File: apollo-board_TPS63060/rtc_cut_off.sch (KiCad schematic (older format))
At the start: 17 parts, among them J6 Conn_01x02_Male, Q6 BSS84-7-F, SW1 DNP/SKRKAEE020, U5 RV-3028-C7, U8 TPS70933DRVT

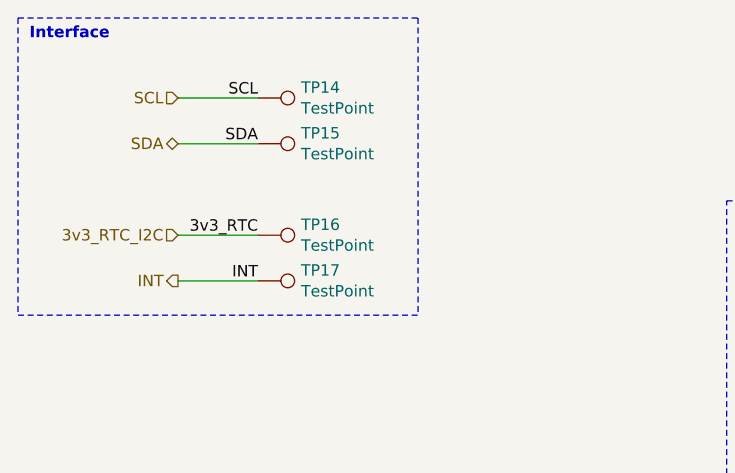
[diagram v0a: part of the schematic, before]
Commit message: Remove unused parts at schematic level.
+ solve schematic DRC issues
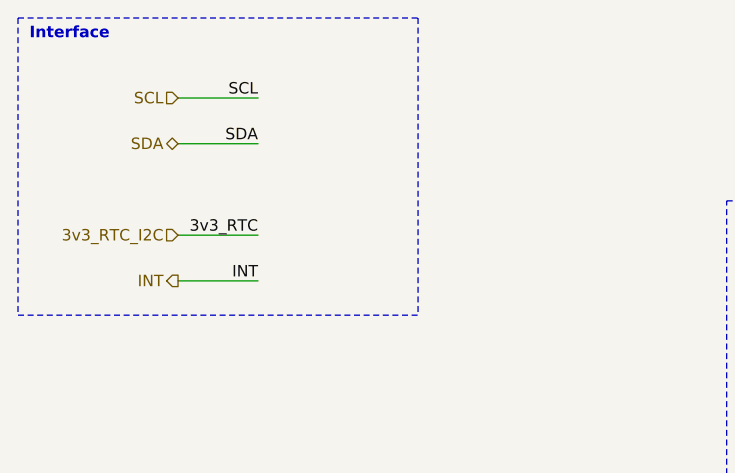
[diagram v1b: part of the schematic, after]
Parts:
- removed TP14, TP15, TP16, TP17: TestPoint, TestPoint:TestPoint_Pad_D1.0mm, symbol Connector:TestPoint
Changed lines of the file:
@@
 Text Notes 6400 1750 2    50   Italic 0
 External trigger\nswitch on board (optional)
-$Comp
-L Connector:TestPoint TP14
-U 1 1 5FD6FC2A
-P 1600 900
-F 0 "TP14" V 1554 1088 50  0000 L CNN
-F 1 "TestPoint" V 1645 1088 50  0000 L CNN
-F 2 "TestPoint:TestPoint_Pad_D1.0mm" H 1800 900 50  0001 C CNN
-F 3 "~" H 1800 900 50  0001 C CNN
-	1    1600 900
-	0    1    1    0
-$EndComp
-$Comp
-L Connector:TestPoint TP15
-U 1 1 5FD6FEB6
-P 1600 1100
-F 0 "TP15" V 1554 1288 50  0000 L CNN
-F 1 "TestPoint" V 1645 1288 50  0000 L CNN
-F 2 "TestPoint:TestPoint_Pad_D1.0mm" H 1800 1100 50  0001 C CNN
-F 3 "~" H 1800 1100 50  0001 C CNN
-	1    1600 1100
-	0    1    1    0
-$EndComp
-$Comp
-L Connector:TestPoint TP16
-U 1 1 5FD700CA
-P 1600 1500
-F 0 "TP16" V 1554 1688 50  0000 L CNN
-F 1 "TestPoint" V 1645 1688 50  0000 L CNN
-F 2 "TestPoint:TestPoint_Pad_D1.0mm" H 1800 1500 50  0001 C CNN
-F 3 "~" H 1800 1500 50  0001 C CNN
-	1    1600 1500
-	0    1    1    0
-$EndComp
-$Comp
-L Connector:TestPoint TP17
-U 1 1 5FD702E9
-P 1600 1700
-F 0 "TP17" V 1554 1888 50  0000 L CNN
-F 1 "TestPoint" V 1645 1888 50  0000 L CNN
-F 2 "TestPoint:TestPoint_Pad_D1.0mm" H 1800 1700 50  0001 C CNN
-F 3 "~" H 1800 1700 50  0001 C CNN
-	1    1600 1700
-	0    1    1    0
-$EndComp
 Wire Notes Line
 	550  550  2300 550

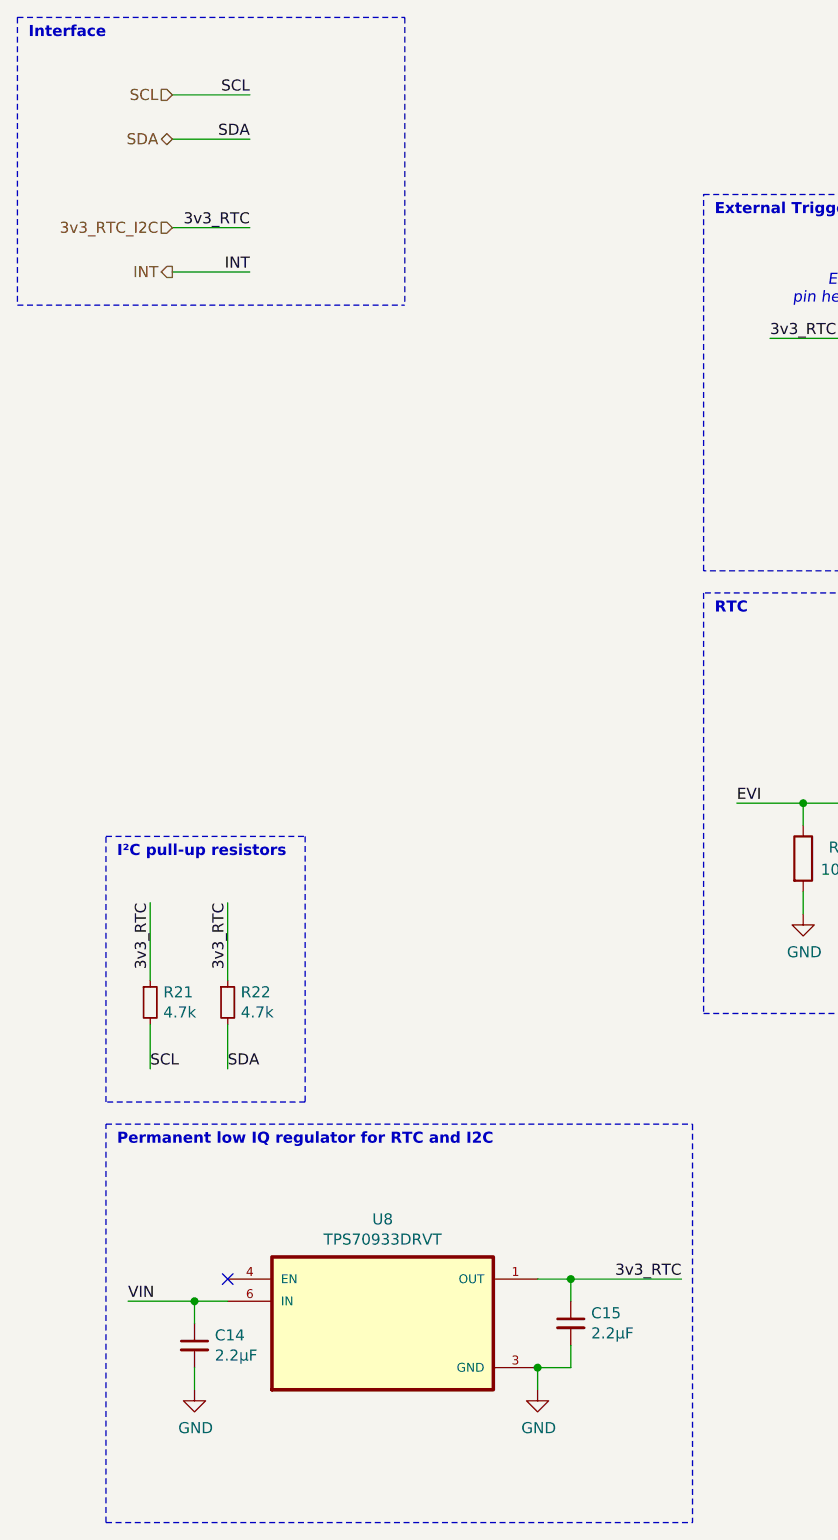
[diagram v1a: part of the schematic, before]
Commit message: Recreate TPS709 symbol to and set footprint to SOT23-5
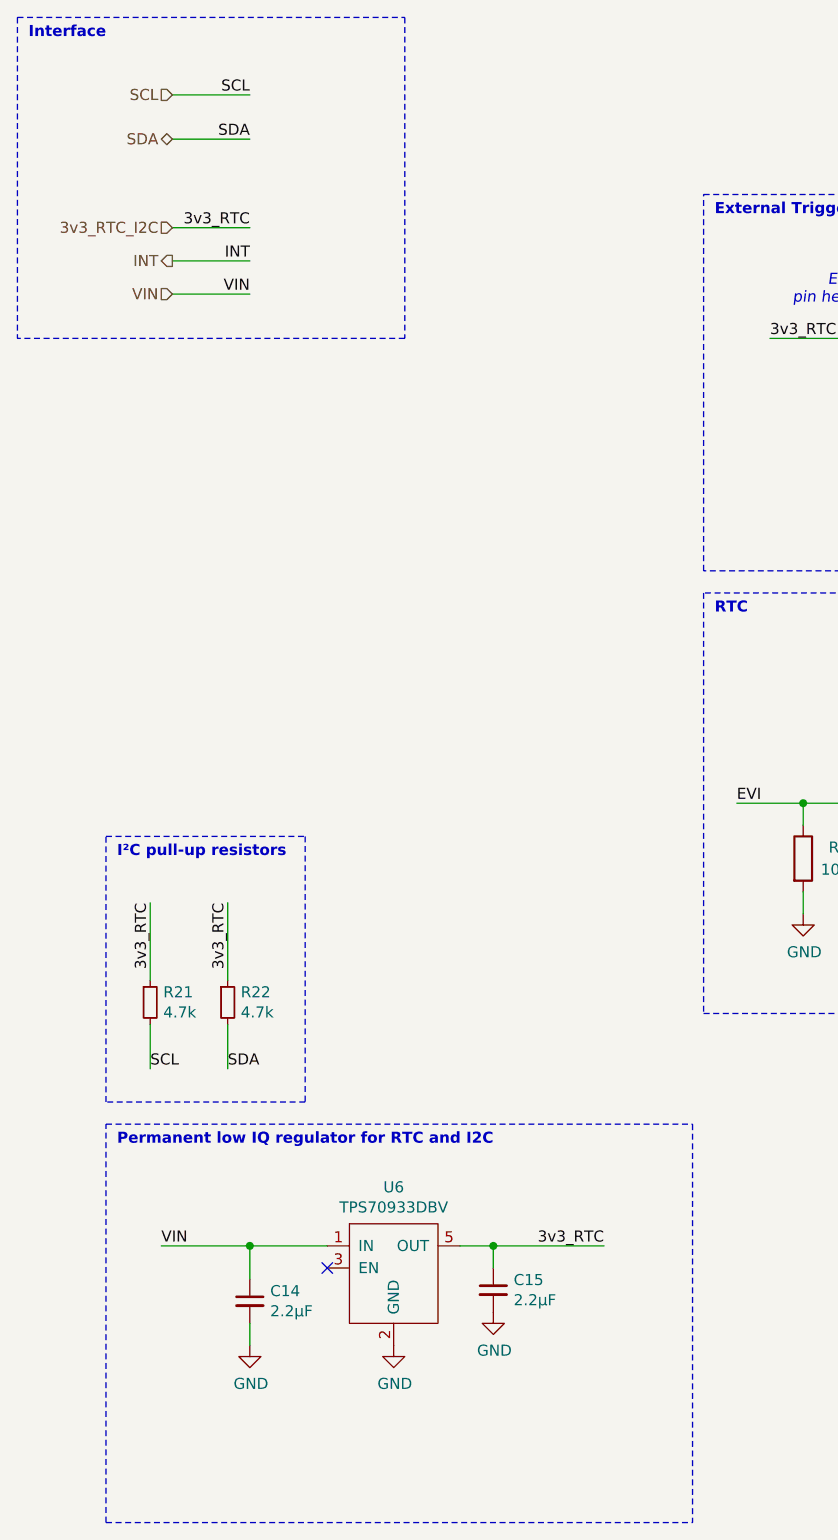
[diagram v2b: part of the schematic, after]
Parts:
- removed U8: TPS70933DRVT, Package_TO_SOT_SMD:SOT-23-6, symbol TPS70933DRV:TPS70933DRVT
- added U6: TPS70933DBV, Package_TO_SOT_SMD:SOT-23-5, symbol TPS70933DRV:TPS70933DBV
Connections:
- net 3v3_RTC_I2C: now also U6.5 (OUT)
- net GND: now also U6.2 (GND)
- net VIN: now also U6.1 (IN)
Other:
- moved on the sheet: C14, C15
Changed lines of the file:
@@
 Text HLabel 1250 1100 0    50   BiDi ~ 0
 SDA
-Text HLabel 1250 1700 0    50   Output ~ 0
+Text HLabel 1250 1650 0    50   Output ~ 0
 INT
 NoConn ~ 6150 4300
@@
 Text Label 1600 1100 2    50   ~ 0
 SDA
-Text Label 1600 1700 2    50   ~ 0
+Text Label 1600 1650 2    50   ~ 0
 INT
 Wire Wire Line
-	1250 1700 1600 1700
+	1250 1650 1600 1650
 Wire Wire Line
 	1250 900  1600 900
@@
 Wire Notes Line
 	550  550  2300 550
-Wire Notes Line
-	2300 550  2300 1850
-Wire Notes Line
-	550  1850 2300 1850
-Wire Notes Line
-	550  550  550  1850
 Text Label 7350 3550 2    50   ~ 0
 3v3_RTC
@@
 	6900 3550 6250 3550
 Connection ~ 6900 3550
-Wire Wire Line
-	1350 6350 1500 6350
-Wire Wire Line
-	1050 6350 1350 6350
-Text Label 1050 6350 0    50   ~ 0
-VIN
-Connection ~ 1350 6350
-Wire Wire Line
-	1350 6350 1350 6450
-$Comp
-L power:GND #PWR?
-U 1 1 5FE9A849
-P 1350 6750
-AR Path="/5F63A0E9/5FE9A849" Ref="#PWR?"  Part="1"
-AR Path="/5F63A00B/5FE9A849" Ref="#PWR0102"  Part="1"
-F 0 "#PWR0102" H 1350 6500 50  0001 C CNN
-F 1 "GND" H 1355 6577 50  0000 C CNN
-F 2 "" H 1350 6750 50  0001 C CNN
-F 3 "" H 1350 6750 50  0001 C CNN
-	1    1350 6750
-	1    0    0    -1
-$EndComp
-$Comp
-L power:GND #PWR?
-U 1 1 5FE9A84F
-P 2900 6750
-AR Path="/5F63A0E9/5FE9A84F" Ref="#PWR?"  Part="1"
-AR Path="/5F63A00B/5FE9A84F" Ref="#PWR0103"  Part="1"
-F 0 "#PWR0103" H 2900 6500 50  0001 C CNN
-F 1 "GND" H 2905 6577 50  0000 C CNN
-F 2 "" H 2900 6750 50  0001 C CNN
-F 3 "" H 2900 6750 50  0001 C CNN
-	1    2900 6750
-	1    0    0    -1
-$EndComp
-Text Label 3550 6250 2    50   ~ 0
-3v3_RTC
-Wire Wire Line
-	3050 6550 3050 6650
-Wire Wire Line
-	3050 6650 2900 6650
-Connection ~ 2900 6650
-Wire Wire Line
-	3050 6350 3050 6250
-Wire Wire Line
-	2900 6750 2900 6650
-Wire Wire Line
-	1350 6650 1350 6750
-NoConn ~ 1500 6250
-Wire Notes Line
-	950  7350 950  5550
-Wire Wire Line
-	2900 6250 3050 6250
-Connection ~ 3050 6250
-$Comp
-L Device:C_Small C?
-U 1 1 5FE9A860
-P 3050 6450
-AR Path="/5F63A0E9/5FE9A860" Ref="C?"  Part="1"
-AR Path="/5F63A00B/5FE9A860" Ref="C15"  Part="1"
-F 0 "C15" H 3142 6496 50  0000 L CNN
-F 1 "2.2μF" H 3142 6405 50  0000 L CNN
-F 2 "Capacitor_SMD:C_0603_1608Metric" H 3050 6450 50  0001 C CNN
-F 3 "~" H 3050 6450 50  0001 C CNN
-	1    3050 6450
-	1    0    0    -1
-$EndComp
-$Comp
-L Device:C_Small C?
-U 1 1 5FE9A866
-P 1350 6550
-AR Path="/5F63A0E9/5FE9A866" Ref="C?"  Part="1"
-AR Path="/5F63A00B/5FE9A866" Ref="C14"  Part="1"
-F 0 "C14" H 1442 6596 50  0000 L CNN
-F 1 "2.2μF" H 1442 6505 50  0000 L CNN
-F 2 "Capacitor_SMD:C_0603_1608Metric" H 1350 6550 50  0001 C CNN
-F 3 "~" H 1350 6550 50  0001 C CNN
-	1    1350 6550
-	1    0    0    -1
-$EndComp
-$Comp
-L TPS70933DRV:TPS70933DRVT U?
-U 1 1 5FE9A86C
-P 2200 6450
-AR Path="/5F63A0E9/5FE9A86C" Ref="U?"  Part="1"
-AR Path="/5F63A00B/5FE9A86C" Ref="U8"  Part="1"
-F 0 "U8" H 2200 6920 50  0000 C CNN
-F 1 "TPS70933DRVT" H 2200 6829 50  0000 C CNN
-F 2 "Package_TO_SOT_SMD:SOT-23-6" H 2200 6450 50  0001 L BNN
-F 3 "https://www.ti.com/lit/gpn/tps709" H 2200 6450 50  0001 L BNN
-	1    2200 6450
-	1    0    0    -1
-$EndComp
-Wire Wire Line
-	3050 6250 3550 6250
-Text Notes 1000 5650 0    50   ~ 10
-Permanent low IQ regulator for RTC and I2C
-Wire Notes Line
-	950  7350 3600 7350
-Wire Notes Line
-	950  5550 3600 5550
-Wire Notes Line
-	3600 5550 3600 7350
 Wire Notes Line
 	7500 5050 7500 3150
@@
 Text Notes 7650 3300 0    50   ~ 10
 Reverse ~INT~ of the RTC
+Wire Notes Line
+	3600 5550 3600 7350
+Wire Notes Line
+	950  5550 3600 5550
+Wire Notes Line
+	950  7350 3600 7350
+Text Notes 1000 5650 0    50   ~ 10
+Permanent low IQ regulator for RTC and I2C
+$Comp
+L Device:C_Small C?
+U 1 1 5FE9A866
+P 1600 6350
+AR Path="/5F63A0E9/5FE9A866" Ref="C?"  Part="1"
+AR Path="/5F63A00B/5FE9A866" Ref="C14"  Part="1"
+F 0 "C14" H 1692 6396 50  0000 L CNN
+F 1 "2.2μF" H 1692 6305 50  0000 L CNN
+F 2 "Capacitor_SMD:C_0603_1608Metric" H 1600 6350 50  0001 C CNN
+F 3 "~" H 1600 6350 50  0001 C CNN
+	1    1600 6350
+	1    0    0    -1
+$EndComp
+$Comp
+L Device:C_Small C?
+U 1 1 5FE9A860
+P 2700 6300
+AR Path="/5F63A0E9/5FE9A860" Ref="C?"  Part="1"
+AR Path="/5F63A00B/5FE9A860" Ref="C15"  Part="1"
+F 0 "C15" H 2792 6346 50  0000 L CNN
+F 1 "2.2μF" H 2792 6255 50  0000 L CNN
+F 2 "Capacitor_SMD:C_0603_1608Metric" H 2700 6300 50  0001 C CNN
+F 3 "~" H 2700 6300 50  0001 C CNN
+	1    2700 6300
+	1    0    0    -1
+$EndComp
+Wire Notes Line
+	950  7350 950  5550
+Wire Wire Line
+	1600 6450 1600 6550
+Wire Wire Line
+	2700 6100 3200 6100
+Wire Wire Line
+	2550 6100 2700 6100
+Connection ~ 2700 6100
+Wire Wire Line
+	2700 6200 2700 6100
+Text Label 3200 6100 2    50   ~ 0
+3v3_RTC
+$Comp
+L power:GND #PWR?
+U 1 1 5FE9A84F
+P 2700 6400
+AR Path="/5F63A0E9/5FE9A84F" Ref="#PWR?"  Part="1"
+AR Path="/5F63A00B/5FE9A84F" Ref="#PWR0103"  Part="1"
+F 0 "#PWR0103" H 2700 6150 50  0001 C CNN
+F 1 "GND" H 2705 6227 50  0000 C CNN
+F 2 "" H 2700 6400 50  0001 C CNN
+F 3 "" H 2700 6400 50  0001 C CNN
+	1    2700 6400
+	1    0    0    -1
+$EndComp
+$Comp
+L power:GND #PWR?
+U 1 1 5FE9A849
+P 1600 6550
+AR Path="/5F63A0E9/5FE9A849" Ref="#PWR?"  Part="1"
+AR Path="/5F63A00B/5FE9A849" Ref="#PWR0102"  Part="1"
+F 0 "#PWR0102" H 1600 6300 50  0001 C CNN
+F 1 "GND" H 1605 6377 50  0000 C CNN
+F 2 "" H 1600 6550 50  0001 C CNN
+F 3 "" H 1600 6550 50  0001 C CNN
+	1    1600 6550
+	1    0    0    -1
+$EndComp
+Text Label 1200 6100 0    50   ~ 0
+VIN
+Text HLabel 1250 1800 0    50   Input ~ 0
+VIN
+Text Label 1600 1800 2    50   ~ 0
+VIN
+Wire Wire Line
+	1250 1800 1600 1800
+Wire Notes Line
+	2300 2000 550  2000
+Wire Notes Line
+	2300 550  2300 2000
+Wire Notes Line
+	550  550  550  2000
+$Comp
+L TPS70933DRV:TPS70933DBV U6
+U 1 1 60CA0347
+P 2250 6200
+F 0 "U6" H 2250 6565 50  0000 C CNN
+F 1 "TPS70933DBV" H 2250 6474 50  0000 C CNN
+F 2 "Package_TO_SOT_SMD:SOT-23-5" H 2250 6200 50  0001 C CNN
+F 3 "" H 2250 6200 50  0001 C CNN
+	1    2250 6200
+	1    0    0    -1
+$EndComp
+$Comp
+L power:GND #PWR?
+U 1 1 60CA31D6
+P 2250 6550
+AR Path="/5F63A0E9/60CA31D6" Ref="#PWR?"  Part="1"
+AR Path="/5F63A00B/60CA31D6" Ref="#PWR0112"  Part="1"
+F 0 "#PWR0112" H 2250 6300 50  0001 C CNN
+F 1 "GND" H 2255 6377 50  0000 C CNN
+F 2 "" H 2250 6550 50  0001 C CNN
+F 3 "" H 2250 6550 50  0001 C CNN
+	1    2250 6550
+	1    0    0    -1
+$EndComp
+Wire Wire Line
+	1200 6100 1600 6100
+Wire Wire Line
+	1600 6250 1600 6100
+Connection ~ 1600 6100
+Wire Wire Line
+	1600 6100 1950 6100
+NoConn ~ 1950 6200
 $EndSCHEMATC

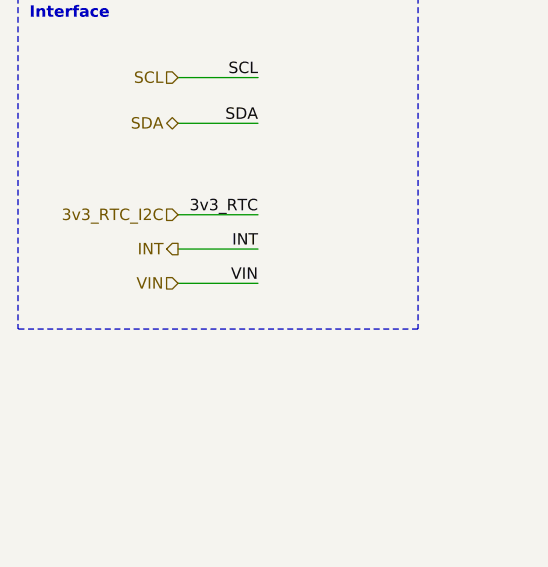
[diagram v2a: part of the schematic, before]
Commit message: Rename some power signal on Schematic to improve readability.
+ Misc. updates
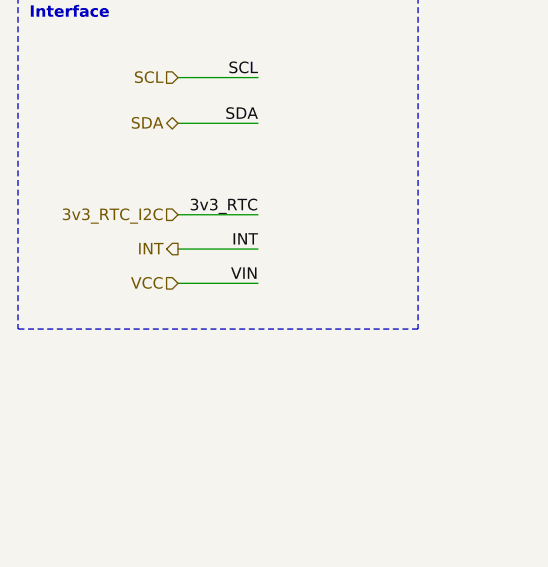
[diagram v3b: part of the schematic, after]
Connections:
- net VIN renamed VCC
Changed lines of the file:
@@
 VIN
 Text HLabel 1250 1800 0    50   Input ~ 0
-VIN
+VCC
 Text Label 1600 1800 2    50   ~ 0
 VIN
